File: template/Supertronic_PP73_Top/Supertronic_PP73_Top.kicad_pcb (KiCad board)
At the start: 2 copper layers, 58 x 58 mm, 4 parts

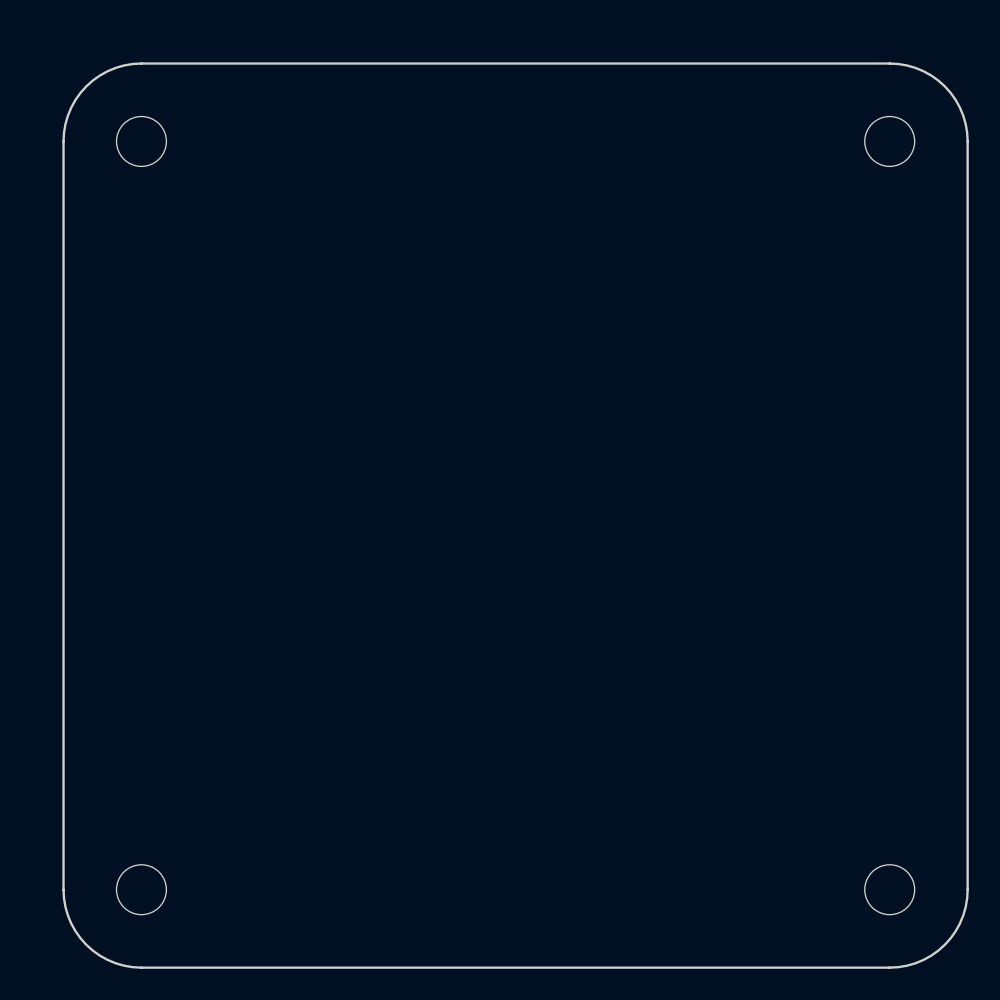
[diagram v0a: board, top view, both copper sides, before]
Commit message: Updated templates
Added mounting holes on schematics, dimensions and re-adjusted board
sizes
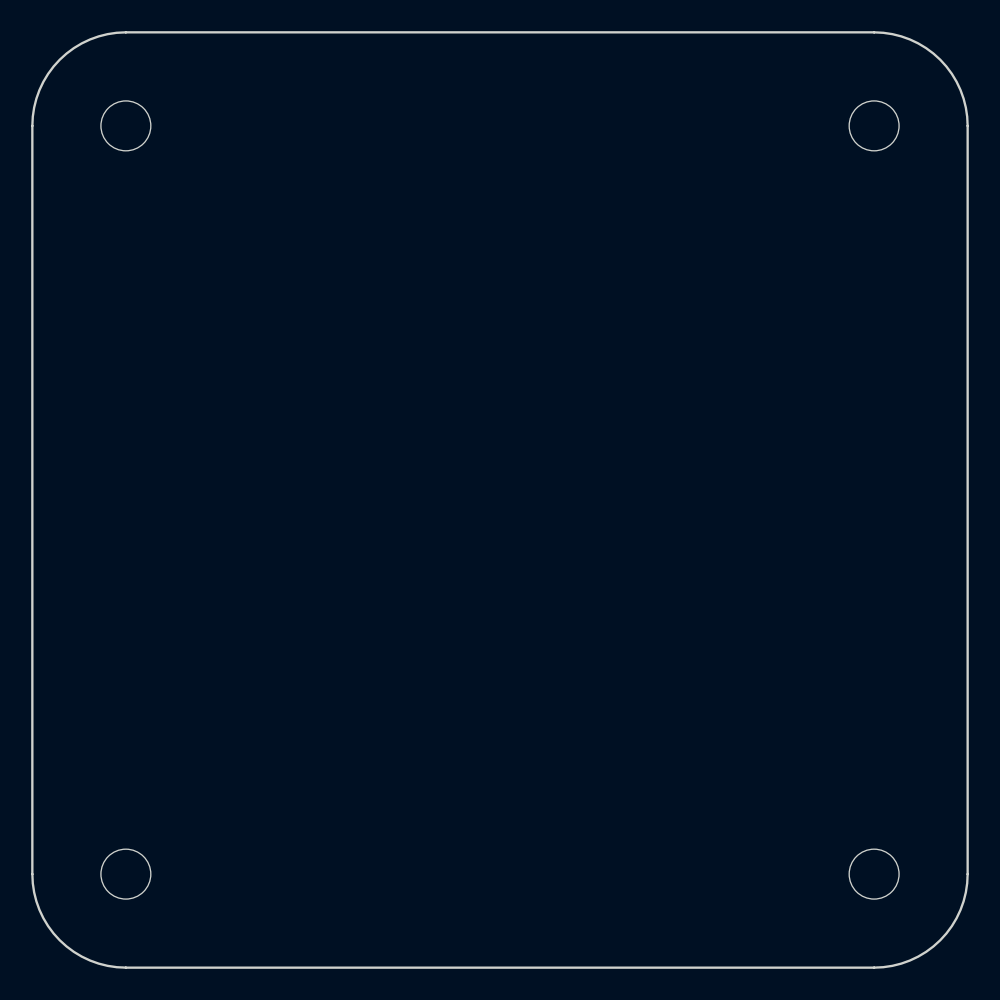
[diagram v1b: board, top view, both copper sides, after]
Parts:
- moved H1 1.41 mm to (121.0, 71.0)
- moved H2 1.41 mm to (169.0, 71.0)
- moved H3 1.41 mm to (169.0, 119.0)
- moved H4 1.41 mm to (121.0, 119.0)
- renumbered REF** to H1, REF** to H2, REF** to H3, REF** to H4
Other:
- board size 58 x 58 mm -> 60 x 60 mm
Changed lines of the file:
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@@
-(kicad_pcb (version 20171130) (host pcbnew 5.0.1-1.fc29)
+(kicad_pcb (version 20171130) (host pcbnew 5.0.2-1.fc29)
   (general
     (thickness 1.6)
-    (drawings 8)
+    (drawings 11)
     (tracks 0)
     (zones 0)
@@
     (pad_to_mask_clearance 0.051)
     (solder_mask_min_width 0.25)
-    (aux_axis_origin 0 0)
+    (aux_axis_origin 115 125)
+    (grid_origin 115 125)
     (visible_elements FFFFFF7F)
     (pcbplotparams
@@
   )
   (module MountingHole:MountingHole_3.2mm_M3 locked (layer F.Cu)
-    (at 122 120)
-    (descr "Mounting Hole 3.2mm, no annular, M3")
-    (tags "mounting hole 3.2mm no annular m3")
-    (attr virtual)
-    (fp_text reference REF** (at 0 -4.2) (layer F.SilkS) hide
-      (effects (font (size 1 1) (thickness 0.15)))
-    )
-    (fp_text value MountingHole_3.2mm_M3 (at 0 4.2) (layer F.Fab) hide
-      (effects (font (size 1 1) (thickness 0.15)))
-    )
-    (fp_circle (center 0 0) (end 3.45 0) (layer F.CrtYd) (width 0.05))
-    (fp_circle (center 0 0) (end 3.2 0) (layer Cmts.User) (width 0.15))
-    (fp_text user %R (at 0.3 0) (layer F.Fab)
-      (effects (font (size 1 1) (thickness 0.15)))
-    )
-    (pad 1 np_thru_hole circle (at 0 0) (size 3.2 3.2) (drill 3.2) (layers *.Cu *.Mask))
-  )
-  (module MountingHole:MountingHole_3.2mm_M3 locked (layer F.Cu)
-    (at 170 120)
-    (descr "Mounting Hole 3.2mm, no annular, M3")
-    (tags "mounting hole 3.2mm no annular m3")
-    (attr virtual)
-    (fp_text reference REF** (at 0 -4.2) (layer F.SilkS) hide
-      (effects (font (size 1 1) (thickness 0.15)))
-    )
-    (fp_text value MountingHole_3.2mm_M3 (at 0 4.2) (layer F.Fab) hide
-      (effects (font (size 1 1) (thickness 0.15)))
-    )
-    (fp_text user %R (at 0.3 0) (layer F.Fab)
-      (effects (font (size 1 1) (thickness 0.15)))
-    )
-    (fp_circle (center 0 0) (end 3.2 0) (layer Cmts.User) (width 0.15))
-    (fp_circle (center 0 0) (end 3.45 0) (layer F.CrtYd) (width 0.05))
-    (pad 1 np_thru_hole circle (at 0 0) (size 3.2 3.2) (drill 3.2) (layers *.Cu *.Mask))
-  )
-  (module MountingHole:MountingHole_3.2mm_M3 locked (layer F.Cu)
-    (at 122 72)
-    (descr "Mounting Hole 3.2mm, no annular, M3")
-    (tags "mounting hole 3.2mm no annular m3")
-    (attr virtual)
-    (fp_text reference REF** (at 0 -4.2) (layer F.SilkS) hide
-      (effects (font (size 1 1) (thickness 0.15)))
-    )
-    (fp_text value MountingHole_3.2mm_M3 (at 0 4.2) (layer F.Fab) hide
-      (effects (font (size 1 1) (thickness 0.15)))
-    )
-    (fp_circle (center 0 0) (end 3.45 0) (layer F.CrtYd) (width 0.05))
-    (fp_circle (center 0 0) (end 3.2 0) (layer Cmts.User) (width 0.15))
-    (fp_text user %R (at 0.3 0) (layer F.Fab)
-      (effects (font (size 1 1) (thickness 0.15)))
-    )
-    (pad 1 np_thru_hole circle (at 0 0) (size 3.2 3.2) (drill 3.2) (layers *.Cu *.Mask))
-  )
-  (module MountingHole:MountingHole_3.2mm_M3 locked (layer F.Cu)
-    (at 170 72)
-    (descr "Mounting Hole 3.2mm, no annular, M3")
-    (tags "mounting hole 3.2mm no annular m3")
-    (attr virtual)
-    (fp_text reference REF** (at 0 -4.2) (layer F.SilkS) hide
-      (effects (font (size 1 1) (thickness 0.15)))
-    )
-    (fp_text value MountingHole_3.2mm_M3 (at 0 4.2) (layer F.Fab) hide
-      (effects (font (size 1 1) (thickness 0.15)))
-    )
-    (fp_circle (center 0 0) (end 3.45 0) (layer F.CrtYd) (width 0.05))
-    (fp_circle (center 0 0) (end 3.2 0) (layer Cmts.User) (width 0.15))
-    (fp_text user %R (at 0.3 0) (layer F.Fab)
-      (effects (font (size 1 1) (thickness 0.15)))
-    )
-    (pad 1 np_thru_hole circle (at 0 0) (size 3.2 3.2) (drill 3.2) (layers *.Cu *.Mask))
-  )
-  (gr_arc (start 122 72) (end 122 67) (angle -90) (layer Edge.Cuts) (width 0.15))
-  (gr_arc (start 122 120) (end 117 120) (angle -90) (layer Edge.Cuts) (width 0.15))
-  (gr_arc (start 170 120) (end 170 125) (angle -90) (layer Edge.Cuts) (width 0.15))
-  (gr_arc (start 170 72) (end 175 72) (angle -90) (layer Edge.Cuts) (width 0.15))
-  (gr_line (start 117 120) (end 117 72) (layer Edge.Cuts) (width 0.15))
-  (gr_line (start 170 125) (end 122 125) (layer Edge.Cuts) (width 0.15))
-  (gr_line (start 175 72) (end 175 120) (layer Edge.Cuts) (width 0.15))
-  (gr_line (start 122 67) (end 170 67) (layer Edge.Cuts) (width 0.15))
+    (at 121 119)
+    (descr "Mounting Hole 3.2mm, no annular, M3")
+    (tags "mounting hole 3.2mm no annular m3")
+    (attr virtual)
+    (fp_text reference H4 (at 0 -4.2) (layer F.SilkS) hide
+      (effects (font (size 1 1) (thickness 0.15)))
+    )
+    (fp_text value MountingHole_3.2mm_M3 (at 0 4.2) (layer F.Fab) hide
+      (effects (font (size 1 1) (thickness 0.15)))
+    )
+    (fp_circle (center 0 0) (end 3.45 0) (layer F.CrtYd) (width 0.05))
+    (fp_circle (center 0 0) (end 3.2 0) (layer Cmts.User) (width 0.15))
+    (fp_text user %R (at 0.3 0) (layer F.Fab)
+      (effects (font (size 1 1) (thickness 0.15)))
+    )
+    (pad 1 np_thru_hole circle (at 0 0) (size 3.2 3.2) (drill 3.2) (layers *.Cu *.Mask))
+  )
+  (module MountingHole:MountingHole_3.2mm_M3 locked (layer F.Cu)
+    (at 169 119)
+    (descr "Mounting Hole 3.2mm, no annular, M3")
+    (tags "mounting hole 3.2mm no annular m3")
+    (attr virtual)
+    (fp_text reference H3 (at 0 -4.2) (layer F.SilkS) hide
+      (effects (font (size 1 1) (thickness 0.15)))
+    )
+    (fp_text value MountingHole_3.2mm_M3 (at 0 4.2) (layer F.Fab) hide
+      (effects (font (size 1 1) (thickness 0.15)))
+    )
+    (fp_text user %R (at 0.3 0) (layer F.Fab)
+      (effects (font (size 1 1) (thickness 0.15)))
+    )
+    (fp_circle (center 0 0) (end 3.2 0) (layer Cmts.User) (width 0.15))
+    (fp_circle (center 0 0) (end 3.45 0) (layer F.CrtYd) (width 0.05))
+    (pad 1 np_thru_hole circle (at 0 0) (size 3.2 3.2) (drill 3.2) (layers *.Cu *.Mask))
+  )
+  (module MountingHole:MountingHole_3.2mm_M3 locked (layer F.Cu)
+    (at 121 71)
+    (descr "Mounting Hole 3.2mm, no annular, M3")
+    (tags "mounting hole 3.2mm no annular m3")
+    (attr virtual)
+    (fp_text reference H1 (at 0 -4.2) (layer F.SilkS) hide
+      (effects (font (size 1 1) (thickness 0.15)))
+    )
+    (fp_text value MountingHole_3.2mm_M3 (at 0 4.2) (layer F.Fab) hide
+      (effects (font (size 1 1) (thickness 0.15)))
+    )
+    (fp_circle (center 0 0) (end 3.45 0) (layer F.CrtYd) (width 0.05))
+    (fp_circle (center 0 0) (end 3.2 0) (layer Cmts.User) (width 0.15))
+    (fp_text user %R (at 0.3 0) (layer F.Fab)
+      (effects (font (size 1 1) (thickness 0.15)))
+    )
+    (pad 1 np_thru_hole circle (at 0 0) (size 3.2 3.2) (drill 3.2) (layers *.Cu *.Mask))
+  )
+  (module MountingHole:MountingHole_3.2mm_M3 locked (layer F.Cu)
+    (at 169 71)
+    (descr "Mounting Hole 3.2mm, no annular, M3")
+    (tags "mounting hole 3.2mm no annular m3")
+    (attr virtual)
+    (fp_text reference H2 (at 0 -4.2) (layer F.SilkS) hide
+      (effects (font (size 1 1) (thickness 0.15)))
+    )
+    (fp_text value MountingHole_3.2mm_M3 (at 0 4.2) (layer F.Fab) hide
+      (effects (font (size 1 1) (thickness 0.15)))
+    )
+    (fp_circle (center 0 0) (end 3.45 0) (layer F.CrtYd) (width 0.05))
+    (fp_circle (center 0 0) (end 3.2 0) (layer Cmts.User) (width 0.15))
+    (fp_text user %R (at 0.3 0) (layer F.Fab)
+      (effects (font (size 1 1) (thickness 0.15)))
+    )
+    (pad 1 np_thru_hole circle (at 0 0) (size 3.2 3.2) (drill 3.2) (layers *.Cu *.Mask))
+  )
+  (gr_arc (start 169 71) (end 175 71) (angle -90) (layer Edge.Cuts) (width 0.15))
+  (gr_arc (start 121 71) (end 121 65) (angle -90) (layer Edge.Cuts) (width 0.15))
+  (gr_arc (start 121 119) (end 115 119) (angle -90) (layer Edge.Cuts) (width 0.15))
+  (gr_arc (start 169 119) (end 169 125) (angle -90) (layer Edge.Cuts) (width 0.15))
+  (dimension 60 (width 0.3) (layer Dwgs.User)
+    (gr_text "60.000 mm" (at 182.1 95 270) (layer Dwgs.User)
+      (effects (font (size 1.5 1.5) (thickness 0.3)))
+    )
+    (feature1 (pts (xy 169 125) (xy 180.586421 125)))
+    (feature2 (pts (xy 169 65) (xy 180.586421 65)))
+    (crossbar (pts (xy 180 65) (xy 180 125)))
+    (arrow1a (pts (xy 180 125) (xy 179.413579 123.873496)))
+    (arrow1b (pts (xy 180 125) (xy 180.586421 123.873496)))
+    (arrow2a (pts (xy 180 65) (xy 179.413579 66.126504)))
+    (arrow2b (pts (xy 180 65) (xy 180.586421 66.126504)))
+  )
+  (dimension 60 (width 0.3) (layer Dwgs.User)
+    (gr_text "60.000 mm" (at 145 53.9) (layer Dwgs.User)
+      (effects (font (size 1.5 1.5) (thickness 0.3)))
+    )
+    (feature1 (pts (xy 175 71) (xy 175 55.413579)))
+    (feature2 (pts (xy 115 71) (xy 115 55.413579)))
+    (crossbar (pts (xy 115 56) (xy 175 56)))
+    (arrow1a (pts (xy 175 56) (xy 173.873496 56.586421)))
+    (arrow1b (pts (xy 175 56) (xy 173.873496 55.413579)))
+    (arrow2a (pts (xy 115 56) (xy 116.126504 56.586421)))
+    (arrow2b (pts (xy 115 56) (xy 116.126504 55.413579)))
+  )
+  (dimension 48 (width 0.3) (layer Dwgs.User)
+    (gr_text "48.000 mm" (at 145 58.9) (layer Dwgs.User)
+      (effects (font (size 1.5 1.5) (thickness 0.3)))
+    )
+    (feature1 (pts (xy 169 71) (xy 169 60.413579)))
+    (feature2 (pts (xy 121 71) (xy 121 60.413579)))
+    (crossbar (pts (xy 121 61) (xy 169 61)))
+    (arrow1a (pts (xy 169 61) (xy 167.873496 61.586421)))
+    (arrow1b (pts (xy 169 61) (xy 167.873496 60.413579)))
+    (arrow2a (pts (xy 121 61) (xy 122.126504 61.586421)))
+    (arrow2b (pts (xy 121 61) (xy 122.126504 60.413579)))
+  )
+  (gr_line (start 115 119) (end 115 71) (layer Edge.Cuts) (width 0.15))
+  (gr_line (start 169 125) (end 121 125) (layer Edge.Cuts) (width 0.15))
+  (gr_line (start 175 71) (end 175 119) (layer Edge.Cuts) (width 0.15))
+  (gr_line (start 121 65) (end 169 65) (layer Edge.Cuts) (width 0.15))
 )
